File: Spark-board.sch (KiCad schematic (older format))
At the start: 10 parts

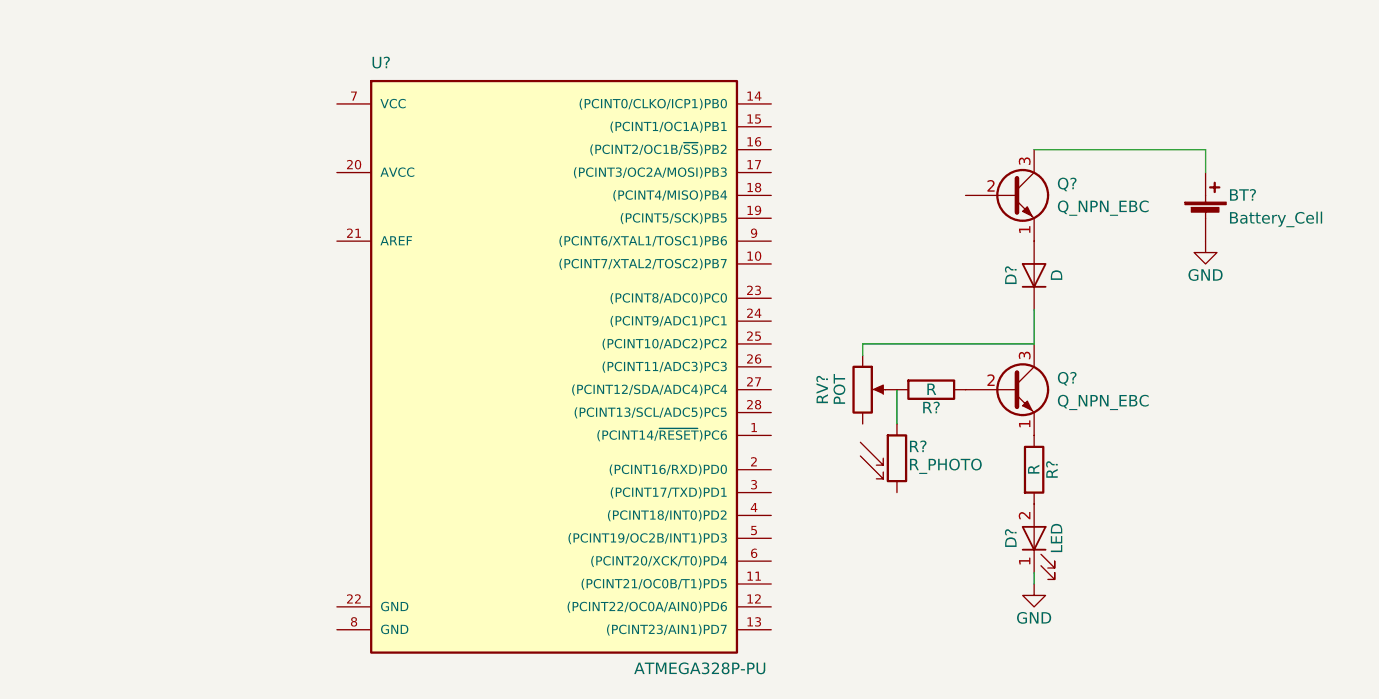
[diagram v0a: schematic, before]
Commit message: - Added hierarchal pin label 'Q1_SWITCH_BASE' and global pin '5V'
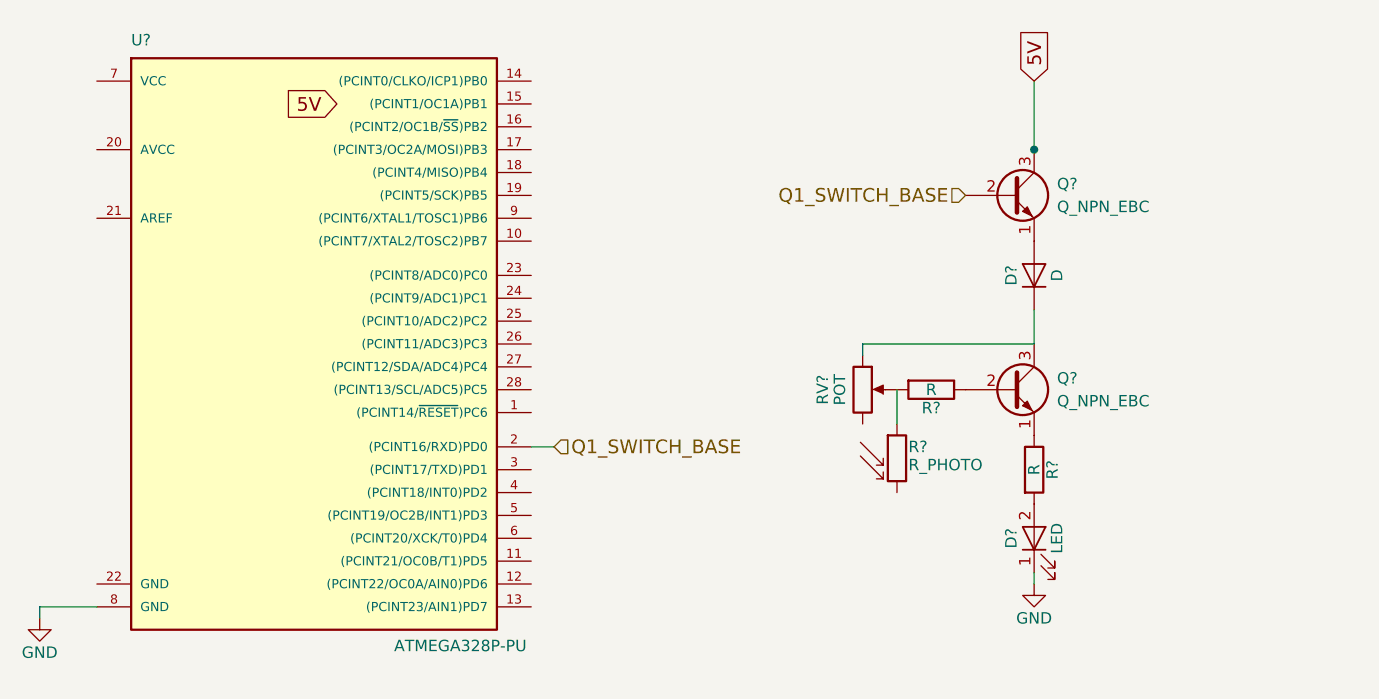
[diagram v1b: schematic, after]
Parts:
- removed BT?: Battery_Cell, symbol Battery_Cell
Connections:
- net GND: now also U?.8 (GND)
- net 5V: now reaches Q?.3 (C)
- net Q1_SWITCH_BASE: now reaches Q?.2 (B)
- net Q1_SWITCH_BASE: now also U?.2 ((PCINT16/RXD)PD0)
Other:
- moved on the sheet: U?
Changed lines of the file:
@@
 LIBS:contrib
 LIBS:valves
+LIBS:Spark-board-cache
 EELAYER 25 0
 EELAYER END
@@
 F 3 "" H 4850 4150 50  0001 C CNN
 	1    4850 4150
-	1    0    0    -1
-$EndComp
-$Comp
-L Battery_Cell BT?
-U 1 1 5BE8E700
-P 6350 3400
-F 0 "BT?" H 6450 3500 50  0000 L CNN
-F 1 "Battery_Cell" H 6450 3400 50  0000 L CNN
-F 2 "" V 6350 3460 50  0001 C CNN
-F 3 "" V 6350 3460 50  0001 C CNN
-	1    6350 3400
 	1    0    0    -1
 $EndComp
@@
 	5000 4300 5000 4150
 $Comp
+L ATMEGA328P-PU U?
+U 1 1 5BE8F131
+P 2400 3900
+F 0 "U?" H 1650 5150 50  0000 L BNN
+F 1 "ATMEGA328P-PU" H 2800 2500 50  0000 L BNN
+F 2 "DIL28" H 2400 3900 50  0001 C CIN
+F 3 "" H 2400 3900 50  0001 C CNN
+	1    2400 3900
+	1    0    0    -1
+$EndComp
+Text GLabel 2550 2900 0    60   Input ~ 0
+5V
+Text GLabel 5600 2800 1    60   Input ~ 0
+5V
+Wire Wire Line
+	5600 2800 5600 3100
+Connection ~ 5600 3100
+$Comp
 L GND #PWR?
-U 1 1 5BE8EFAE
-P 6350 3500
-F 0 "#PWR?" H 6350 3250 50  0001 C CNN
-F 1 "GND" H 6350 3350 50  0000 C CNN
-F 2 "" H 6350 3500 50  0001 C CNN
-F 3 "" H 6350 3500 50  0001 C CNN
-	1    6350 3500
+U 1 1 5BEA3ECB
+P 1250 5150
+F 0 "#PWR?" H 1250 4900 50  0001 C CNN
+F 1 "GND" H 1250 5000 50  0000 C CNN
+F 2 "" H 1250 5150 50  0001 C CNN
+F 3 "" H 1250 5150 50  0001 C CNN
+	1    1250 5150
 	1    0    0    -1
 $EndComp
 Wire Wire Line
-	6350 3200 6350 3100
+	1250 5100 1250 5150
+Text HLabel 3500 4400 2    60   Input ~ 0
+Q1_SWITCH_BASE
+Text HLabel 5300 3300 0    60   Input ~ 0
+Q1_SWITCH_BASE
 Wire Wire Line
-	6350 3100 5600 3100
-$Comp
-L ATMEGA328P-PU U?
-U 1 1 5BE8F131
-P 3450 4000
-F 0 "U?" H 2700 5250 50  0000 L BNN
-F 1 "ATMEGA328P-PU" H 3850 2600 50  0000 L BNN
-F 2 "DIL28" H 3450 4000 50  0001 C CIN
-F 3 "" H 3450 4000 50  0001 C CNN
-	1    3450 4000
-	1    0    0    -1
-$EndComp
+	3400 4400 3500 4400
+Wire Wire Line
+	1500 5100 1250 5100
 $EndSCHEMATC

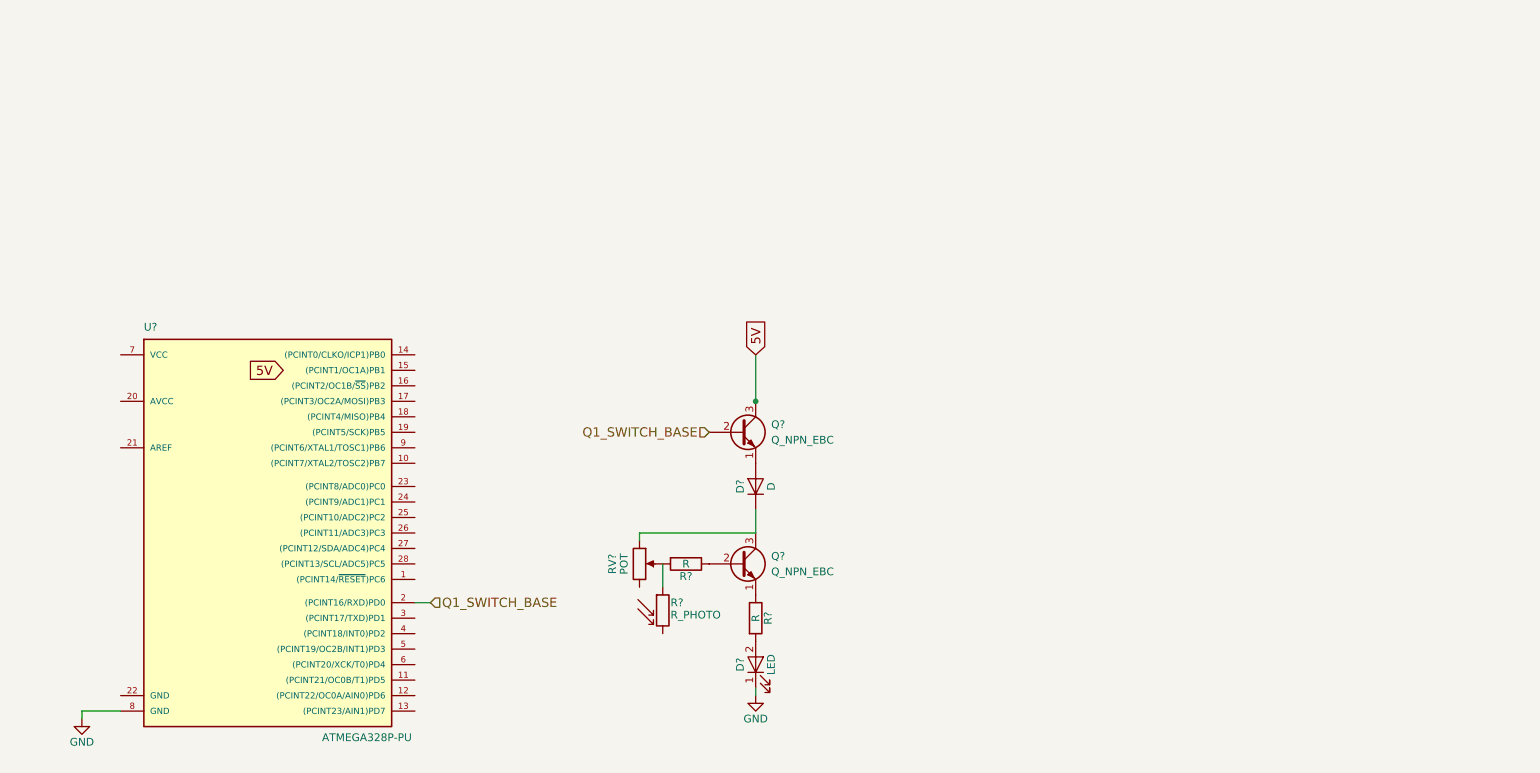
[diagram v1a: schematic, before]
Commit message: - Assigned AVR uP pins to control NPN Transistor
- Added IR Rx Module (TSOP382xx) to allow Power ON/OFF of system remotely
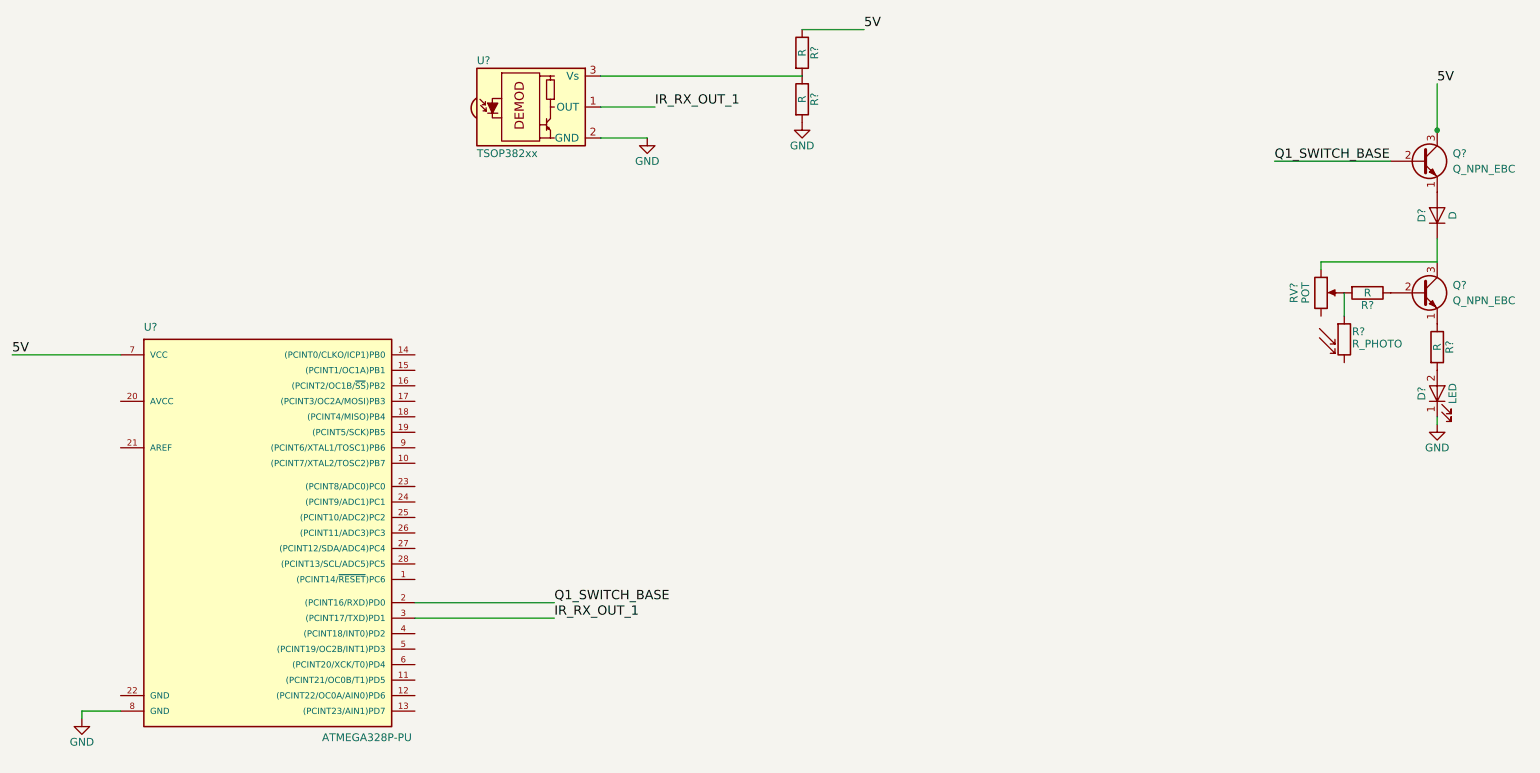
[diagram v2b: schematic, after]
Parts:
- added R? (x2): R, symbol R
- added U?: TSOP382xx, Opto-Devices:IRReceiver_Vishay_MINICAST-3pin, symbol TSOP382xx
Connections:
- net 5V: now also U?.7 (VCC), R?.1
- net GND: now also R?.2, U?.2 (GND)
- net IR_RX_OUT_1: now reaches U?.3 ((PCINT17/TXD)PD1)
- net IR_RX_OUT_1: now also U?.1 (OUT)
- new net: R?.1, R?.2, U?.3 (Vs)
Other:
- moved on the sheet: D?, Q?, R?, RV?
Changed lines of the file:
@@
 L POT RV?
 U 1 1 5BE8E67D
-P 4850 4150
-F 0 "RV?" V 4675 4150 50  0000 C CNN
-F 1 "POT" V 4750 4150 50  0000 C CNN
-F 2 "" H 4850 4150 50  0001 C CNN
-F 3 "" H 4850 4150 50  0001 C CNN
-	1    4850 4150
+P 9250 2400
+F 0 "RV?" V 9075 2400 50  0000 C CNN
+F 1 "POT" V 9150 2400 50  0000 C CNN
+F 2 "" H 9250 2400 50  0001 C CNN
+F 3 "" H 9250 2400 50  0001 C CNN
+	1    9250 2400
 	1    0    0    -1
 $EndComp
@@
 L D D?
 U 1 1 5BE8E73B
-P 5600 3650
-F 0 "D?" H 5600 3750 50  0000 C CNN
-F 1 "D" H 5600 3550 50  0000 C CNN
-F 2 "" H 5600 3650 50  0001 C CNN
-F 3 "" H 5600 3650 50  0001 C CNN
-	1    5600 3650
+P 10000 1900
+F 0 "D?" H 10000 2000 50  0000 C CNN
+F 1 "D" H 10000 1800 50  0000 C CNN
+F 2 "" H 10000 1900 50  0001 C CNN
+F 3 "" H 10000 1900 50  0001 C CNN
+	1    10000 1900
 	0    -1   -1   0
 $EndComp
@@
 L Q_NPN_EBC Q?
 U 1 1 5BE8E792
-P 5500 3300
-F 0 "Q?" H 5700 3350 50  0000 L CNN
-F 1 "Q_NPN_EBC" H 5700 3250 50  0000 L CNN
-F 2 "" H 5700 3400 50  0001 C CNN
-F 3 "" H 5500 3300 50  0001 C CNN
-	1    5500 3300
+P 9900 1550
+F 0 "Q?" H 10100 1600 50  0000 L CNN
+F 1 "Q_NPN_EBC" H 10100 1500 50  0000 L CNN
+F 2 "" H 10100 1650 50  0001 C CNN
+F 3 "" H 9900 1550 50  0001 C CNN
+	1    9900 1550
 	1    0    0    -1
 $EndComp
@@
 L Q_NPN_EBC Q?
 U 1 1 5BE8E8A3
-P 5500 4150
-F 0 "Q?" H 5700 4200 50  0000 L CNN
-F 1 "Q_NPN_EBC" H 5700 4100 50  0000 L CNN
-F 2 "" H 5700 4250 50  0001 C CNN
-F 3 "" H 5500 4150 50  0001 C CNN
-	1    5500 4150
+P 9900 2400
+F 0 "Q?" H 10100 2450 50  0000 L CNN
+F 1 "Q_NPN_EBC" H 10100 2350 50  0000 L CNN
+F 2 "" H 10100 2500 50  0001 C CNN
+F 3 "" H 9900 2400 50  0001 C CNN
+	1    9900 2400
 	1    0    0    -1
 $EndComp
@@
 L R R?
 U 1 1 5BE8EA00
-P 5150 4150
-F 0 "R?" V 5230 4150 50  0000 C CNN
-F 1 "R" V 5150 4150 50  0000 C CNN
-F 2 "" V 5080 4150 50  0001 C CNN
-F 3 "" H 5150 4150 50  0001 C CNN
-	1    5150 4150
+P 9550 2400
+F 0 "R?" V 9630 2400 50  0000 C CNN
+F 1 "R" V 9550 2400 50  0000 C CNN
+F 2 "" V 9480 2400 50  0001 C CNN
+F 3 "" H 9550 2400 50  0001 C CNN
+	1    9550 2400
 	0    1    1    0
 $EndComp
 Wire Wire Line
-	5600 3950 4850 3950
-Wire Wire Line
-	4850 3950 4850 4000
-Wire Wire Line
-	5600 3950 5600 3800
+	10000 2200 9250 2200
+Wire Wire Line
+	9250 2200 9250 2250
+Wire Wire Line
+	10000 2200 10000 2050
 $Comp
 L R R?
 U 1 1 5BE8EB2A
-P 5600 4500
-F 0 "R?" V 5680 4500 50  0000 C CNN
-F 1 "R" V 5600 4500 50  0000 C CNN
-F 2 "" V 5530 4500 50  0001 C CNN
-F 3 "" H 5600 4500 50  0001 C CNN
-	1    5600 4500
+P 10000 2750
+F 0 "R?" V 10080 2750 50  0000 C CNN
+F 1 "R" V 10000 2750 50  0000 C CNN
+F 2 "" V 9930 2750 50  0001 C CNN
+F 3 "" H 10000 2750 50  0001 C CNN
+	1    10000 2750
 	1    0    0    -1
 $EndComp
@@
 L LED D?
 U 1 1 5BE8EB6D
-P 5600 4800
-F 0 "D?" H 5600 4900 50  0000 C CNN
-F 1 "LED" H 5600 4700 50  0000 C CNN
-F 2 "" H 5600 4800 50  0001 C CNN
-F 3 "" H 5600 4800 50  0001 C CNN
-	1    5600 4800
+P 10000 3050
+F 0 "D?" H 10000 3150 50  0000 C CNN
+F 1 "LED" H 10000 2950 50  0000 C CNN
+F 2 "" H 10000 3050 50  0001 C CNN
+F 3 "" H 10000 3050 50  0001 C CNN
+	1    10000 3050
 	0    -1   -1   0
 $EndComp
@@
 L GND #PWR?
 U 1 1 5BE8EDF4
-P 5600 5000
-F 0 "#PWR?" H 5600 4750 50  0001 C CNN
-F 1 "GND" H 5600 4850 50  0000 C CNN
-F 2 "" H 5600 5000 50  0001 C CNN
-F 3 "" H 5600 5000 50  0001 C CNN
-	1    5600 5000
-	1    0    0    -1
-$EndComp
-Wire Wire Line
-	5600 4950 5600 5000
+P 10000 3250
+F 0 "#PWR?" H 10000 3000 50  0001 C CNN
+F 1 "GND" H 10000 3100 50  0000 C CNN
+F 2 "" H 10000 3250 50  0001 C CNN
+F 3 "" H 10000 3250 50  0001 C CNN
+	1    10000 3250
+	1    0    0    -1
+$EndComp
+Wire Wire Line
+	10000 3200 10000 3250
 $Comp
 L R_PHOTO R?
 U 1 1 5BE8EE4E
-P 5000 4450
-F 0 "R?" H 5050 4500 50  0000 L CNN
-F 1 "R_PHOTO" H 5050 4450 50  0000 L TNN
-F 2 "" V 5050 4200 50  0001 L CNN
-F 3 "" H 5000 4400 50  0001 C CNN
-	1    5000 4450
-	1    0    0    -1
-$EndComp
-Wire Wire Line
-	5000 4300 5000 4150
+P 9400 2700
+F 0 "R?" H 9450 2750 50  0000 L CNN
+F 1 "R_PHOTO" H 9450 2700 50  0000 L TNN
+F 2 "" V 9450 2450 50  0001 L CNN
+F 3 "" H 9400 2650 50  0001 C CNN
+	1    9400 2700
+	1    0    0    -1
+$EndComp
+Wire Wire Line
+	9400 2550 9400 2400
 $Comp
 L ATMEGA328P-PU U?
@@
 	1    0    0    -1
 $EndComp
-Text GLabel 2550 2900 0    60   Input ~ 0
-5V
-Text GLabel 5600 2800 1    60   Input ~ 0
-5V
-Wire Wire Line
-	5600 2800 5600 3100
-Connection ~ 5600 3100
+Wire Wire Line
+	10000 1050 10000 1350
+Connection ~ 10000 1350
 $Comp
 L GND #PWR?
@@
 Wire Wire Line
 	1250 5100 1250 5150
-Text HLabel 3500 4400 2    60   Input ~ 0
+Wire Wire Line
+	3400 4400 4300 4400
+Wire Wire Line
+	1500 5100 1250 5100
+Wire Wire Line
+	8950 1550 9700 1550
+Text Label 8950 1550 0    60   ~ 0
 Q1_SWITCH_BASE
-Text HLabel 5300 3300 0    60   Input ~ 0
+Text Label 4300 4400 0    60   ~ 0
 Q1_SWITCH_BASE
-Wire Wire Line
-	3400 4400 3500 4400
-Wire Wire Line
-	1500 5100 1250 5100
+Text Label 10000 1050 0    60   ~ 0
+5V
+Wire Wire Line
+	1500 2800 800  2800
+Text Label 800  2800 0    60   ~ 0
+5V
+$Comp
+L TSOP382xx U?
+U 1 1 5BF22523
+P 4200 1200
+F 0 "U?" H 3800 1500 50  0000 L CNN
+F 1 "TSOP382xx" H 3800 900 50  0000 L CNN
+F 2 "Opto-Devices:IRReceiver_Vishay_MINICAST-3pin" H 4150 825 50  0001 C CNN
+F 3 "" H 4850 1500 50  0001 C CNN
+	1    4200 1200
+	1    0    0    -1
+$EndComp
+$Comp
+L GND #PWR?
+U 1 1 5BF225DA
+P 4900 1400
+F 0 "#PWR?" H 4900 1150 50  0001 C CNN
+F 1 "GND" H 4900 1250 50  0000 C CNN
+F 2 "" H 4900 1400 50  0001 C CNN
+F 3 "" H 4900 1400 50  0001 C CNN
+	1    4900 1400
+	1    0    0    -1
+$EndComp
+Wire Wire Line
+	4600 1400 4900 1400
+$Comp
+L R R?
+U 1 1 5BF22754
+P 5900 1150
+F 0 "R?" V 5980 1150 50  0000 C CNN
+F 1 "R" V 5900 1150 50  0000 C CNN
+F 2 "" V 5830 1150 50  0001 C CNN
+F 3 "" H 5900 1150 50  0001 C CNN
+	1    5900 1150
+	1    0    0    -1
+$EndComp
+$Comp
+L R R?
+U 1 1 5BF227B9
+P 5900 850
+F 0 "R?" V 5980 850 50  0000 C CNN
+F 1 "R" V 5900 850 50  0000 C CNN
+F 2 "" V 5830 850 50  0001 C CNN
+F 3 "" H 5900 850 50  0001 C CNN
+	1    5900 850
+	1    0    0    -1
+$EndComp
+Wire Wire Line
+	5900 700  6300 700
+Text Label 6300 700  0    60   ~ 0
+5V
+$Comp
+L GND #PWR?
+U 1 1 5BF22B42
+P 5900 1300
+F 0 "#PWR?" H 5900 1050 50  0001 C CNN
+F 1 "GND" H 5900 1150 50  0000 C CNN
+F 2 "" H 5900 1300 50  0001 C CNN
+F 3 "" H 5900 1300 50  0001 C CNN
+	1    5900 1300
+	1    0    0    -1
+$EndComp
+Wire Wire Line
+	5900 1000 4600 1000
+Wire Wire Line
+	4600 1200 4950 1200
+Text Label 4950 1200 0    60   ~ 0
+IR_RX_OUT_1
+Wire Wire Line
+	3400 4500 4300 4500
+Text Label 4300 4500 0    60   ~ 0
+IR_RX_OUT_1
 $EndSCHEMATC
